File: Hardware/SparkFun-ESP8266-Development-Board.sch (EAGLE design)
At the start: 67 parts, among them J1 U.FL, Q1 2.5A/30V, Q2 MMBT2222A, U1 ESP8266, U2 MCP73831, U3 AT25SF041-SOIC8, U4 AP2112K-3.3V, U5 ATECC108-SSHDA, Y1 26MHz

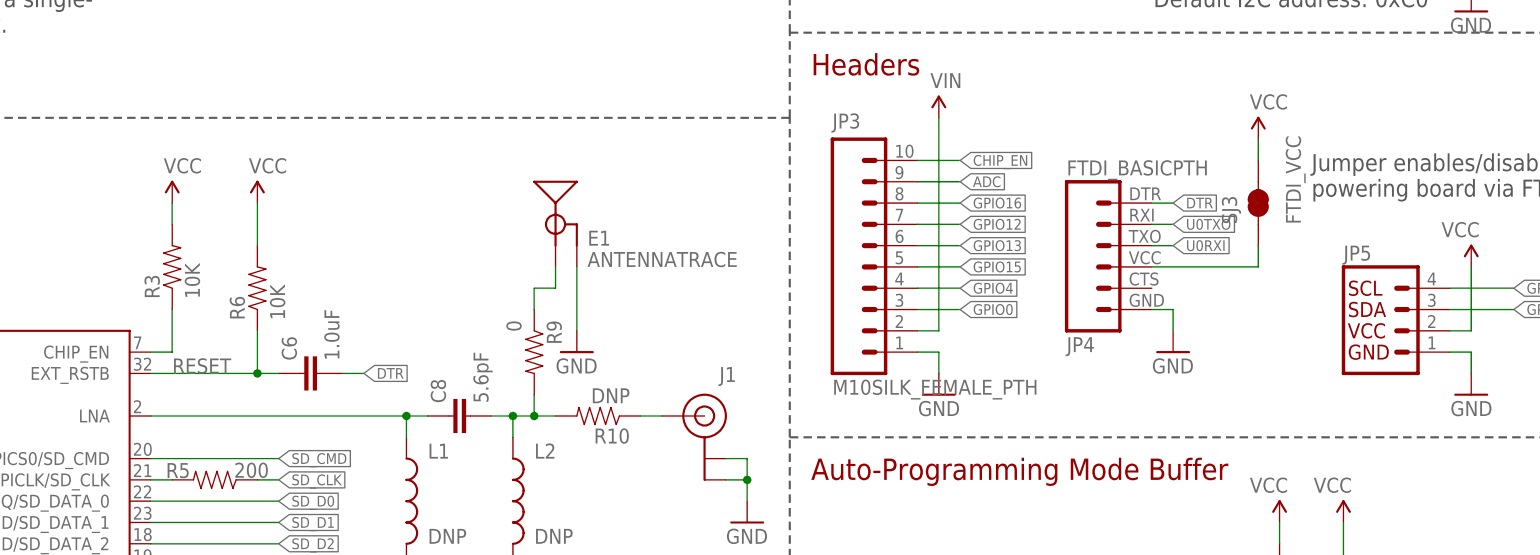
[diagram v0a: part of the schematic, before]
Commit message: Straightening out some nets coming out of ESP8266. Value JP5. Flag label on RESET.
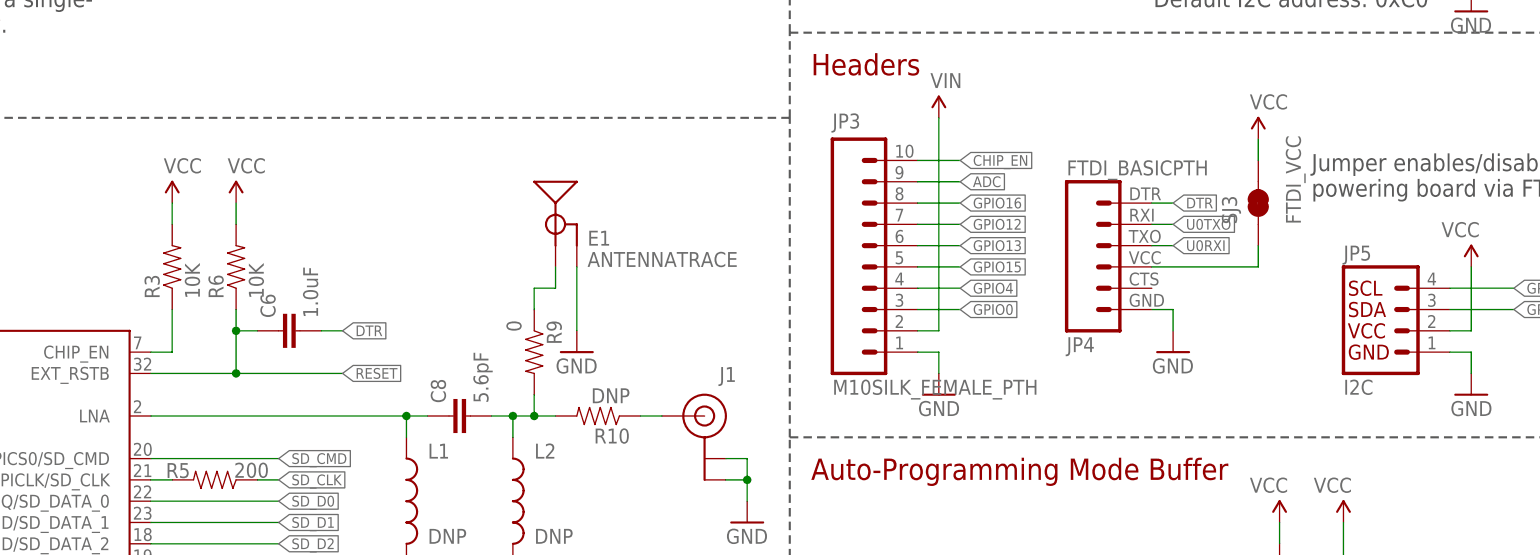
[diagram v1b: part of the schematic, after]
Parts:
- JP5: value (none) -> I2C
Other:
- moved on the sheet: C6, R6

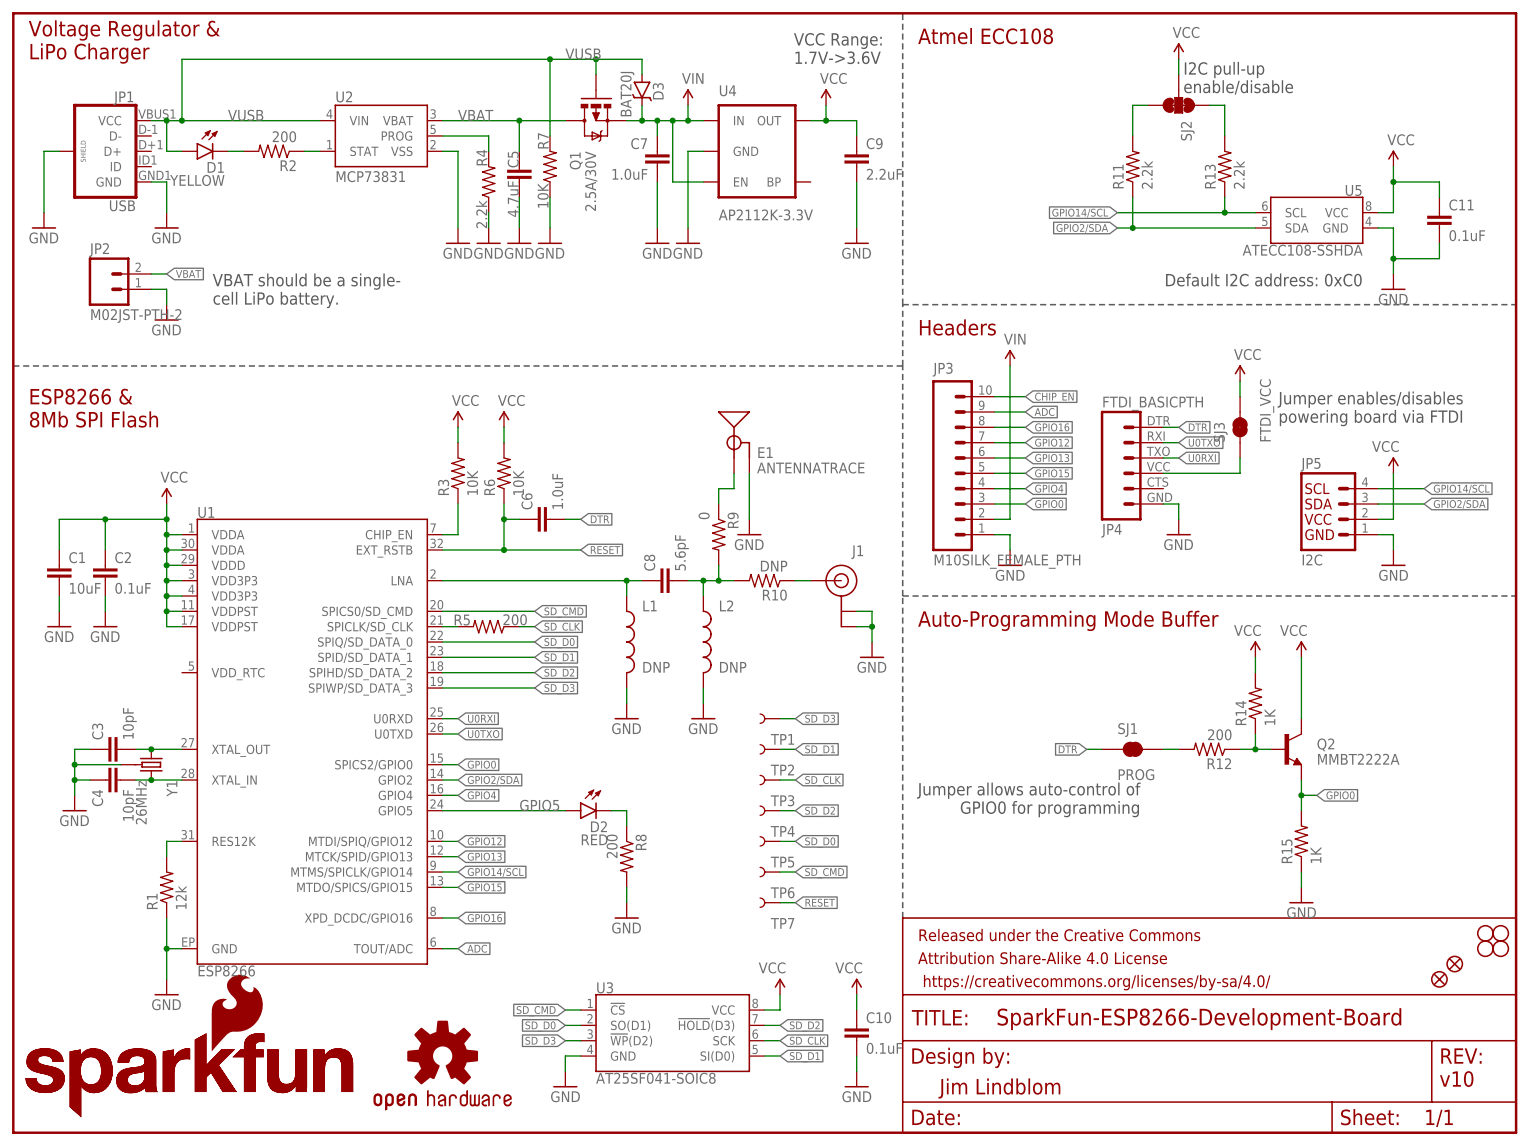
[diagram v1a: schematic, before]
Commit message: Adding power LED. Re-arranging power circuitry. Breaking out pin 5.
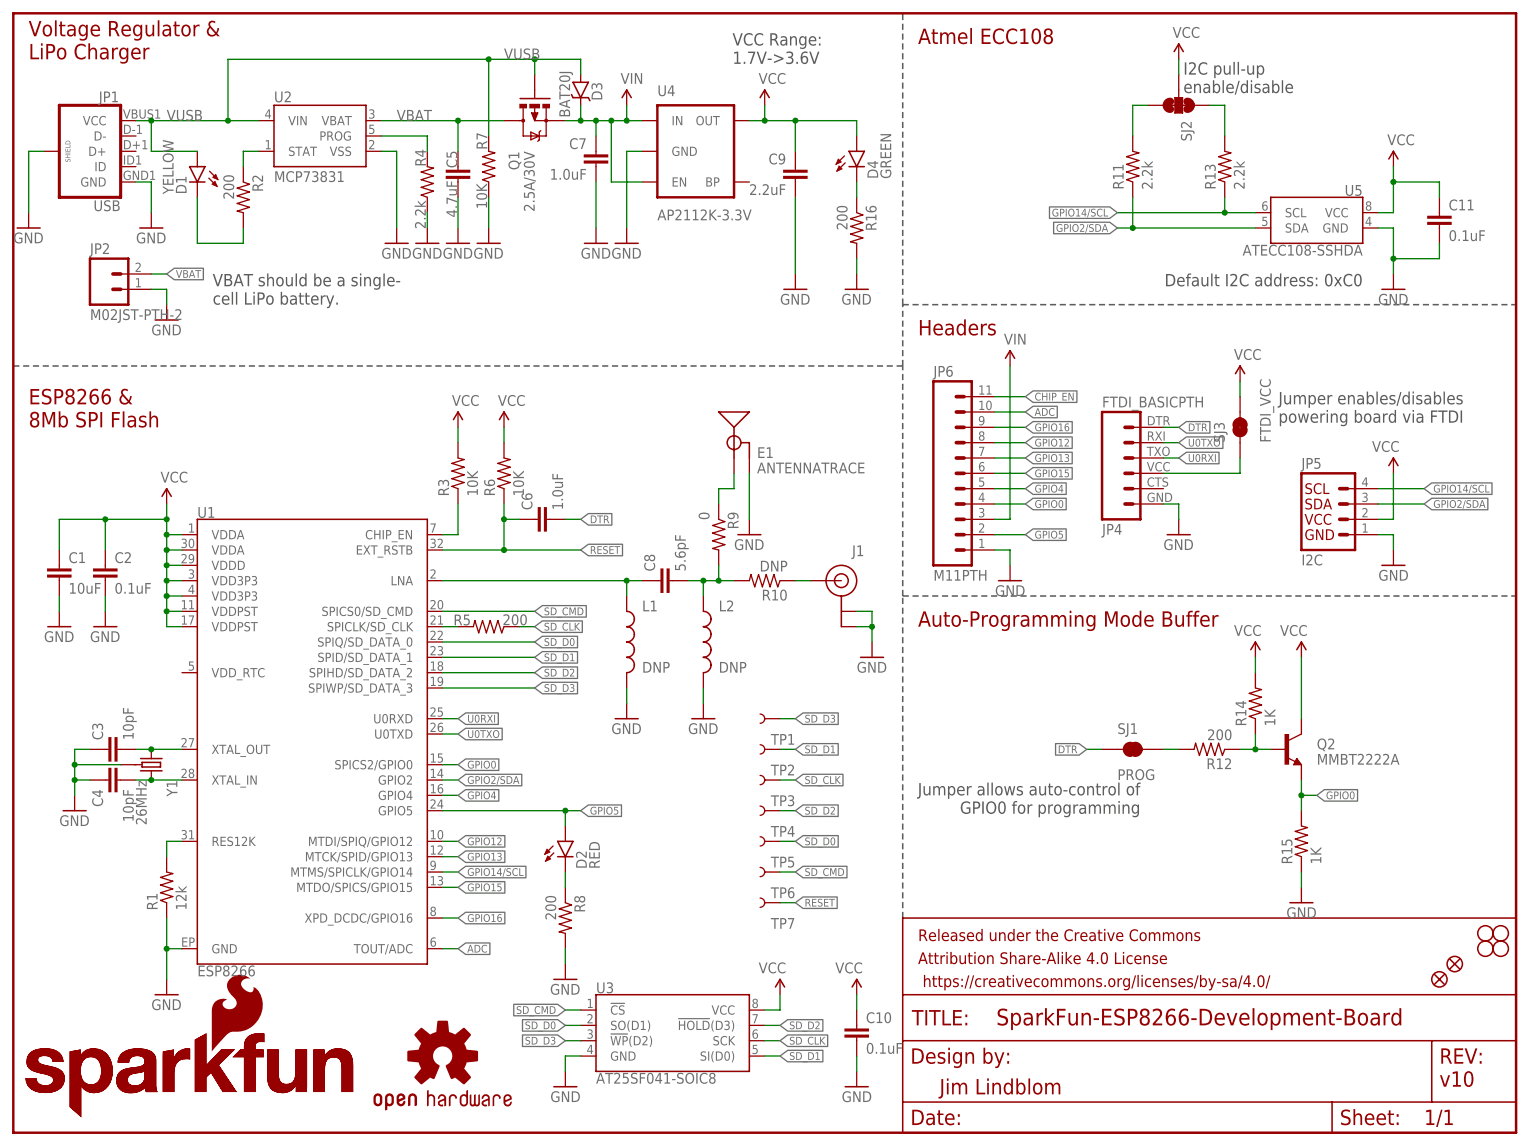
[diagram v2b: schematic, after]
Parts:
- removed JP3: M10SILK_FEMALE_PTH, SparkFun-Connectors:M10SILK_FEMALE_PTH
- added D4: GREEN, SparkFun-LED:LED-GREEN0603
- added JP6: M11PTH, SparkFun-Connectors:M11PTH
- added R16: 200, SparkFun-Resistors:200OHM1/10W1%(0603)
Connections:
- new net N$4: D4.C, R16.1
- net ADC: now also JP6.10; no longer JP3.9
- net CHIP_EN: now also JP6.11; no longer JP3.10
- net GND: now also JP6.1, R16.2; no longer JP3.1
- net GPIO0: now also JP6.4; no longer JP3.3
- net GPIO12: now also JP6.8; no longer JP3.7
- net GPIO13: now also JP6.7; no longer JP3.6
- net GPIO15: now also JP6.6; no longer JP3.5
- net GPIO16: now also JP6.9; no longer JP3.8
- net GPIO4: now also JP6.5; no longer JP3.4
- net GPIO5: now also JP6.2
- net VCC: now also D4.A
- net VIN: now also JP6.3; no longer JP3.2
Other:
- moved on the sheet: C5, C7, C9, D1, D2, D3, JP1, Q1, R2, R4, R7, R8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

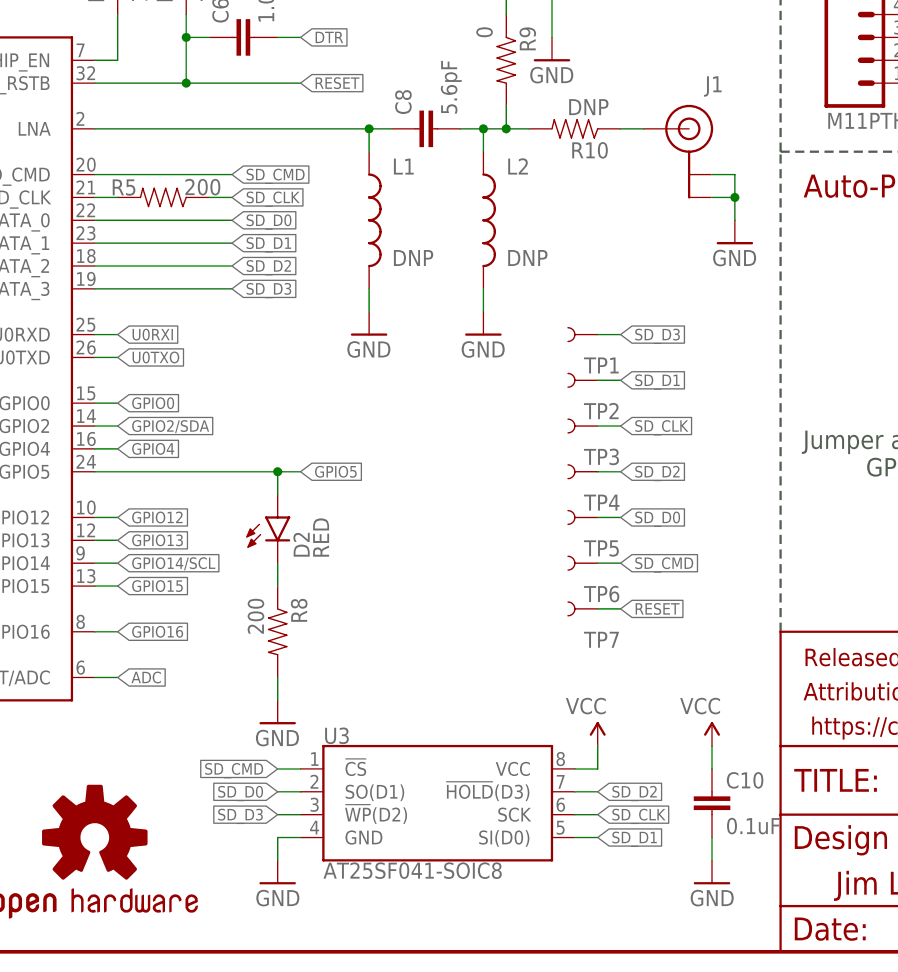
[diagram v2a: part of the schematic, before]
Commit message: Fixing net names for flash signals. Updating bottom silk labels
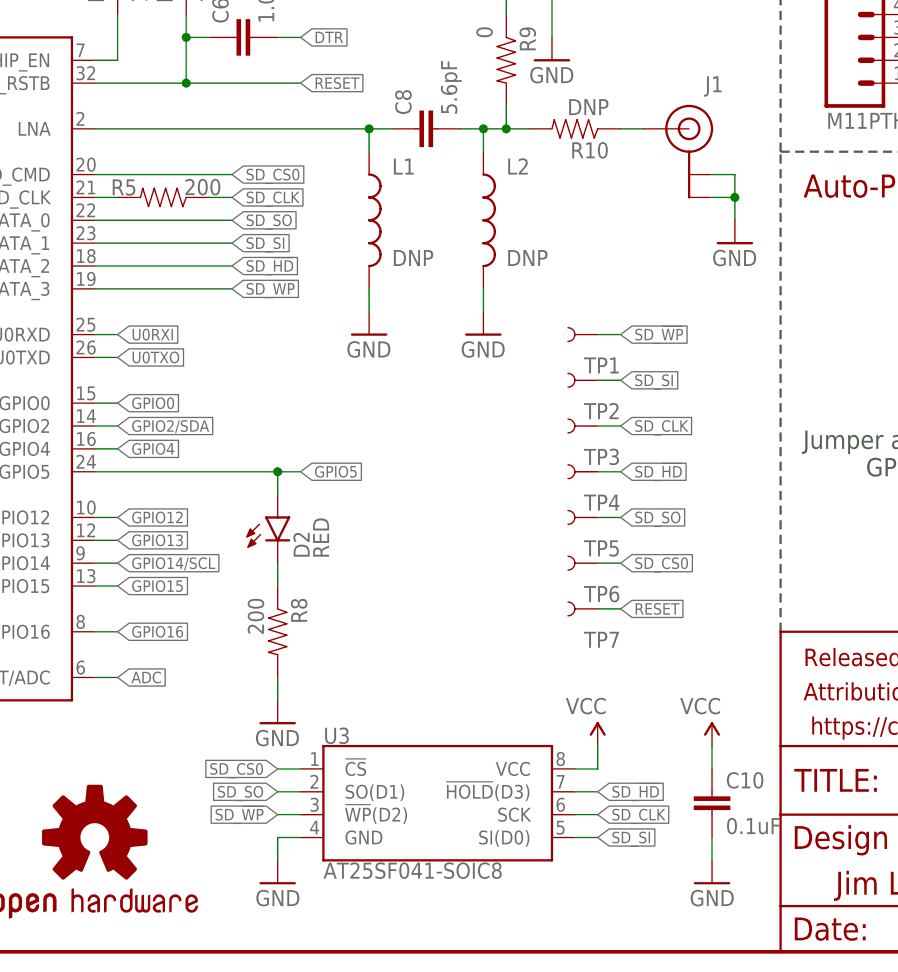
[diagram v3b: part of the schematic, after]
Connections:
- net SD_CMD renamed SD_CS0
- net SD_D0 renamed SD_SO
- net SD_D1 renamed SD_SI
- net SD_D2 renamed SD_!HD!
- net SD_D3 renamed SD_!WP!
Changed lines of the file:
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@@
 </segment>
 </net>
-<net name="SD_D3" class="0">
+<net name="SD_!WP!" class="0">
 <segment>
 <pinref part="U1" gate="G$1" pin="SPIWP/SD_DATA_3"/>
@@
 </segment>
 </net>
-<net name="SD_D2" class="0">
+<net name="SD_!HD!" class="0">
 <segment>
 <pinref part="U1" gate="G$1" pin="SPIHD/SD_DATA_2"/>
@@
 </segment>
 </net>
-<net name="SD_D1" class="0">
+<net name="SD_SI" class="0">
 <segment>
 <pinref part="U1" gate="G$1" pin="SPID/SD_DATA_1"/>
@@
 </segment>
 </net>
-<net name="SD_D0" class="0">
+<net name="SD_SO" class="0">
 <segment>
 <pinref part="U1" gate="G$1" pin="SPIQ/SD_DATA_0"/>
@@
 </segment>
 </net>
-<net name="SD_CMD" class="0">
+<net name="SD_CS0" class="0">
 <segment>
 <pinref part="U1" gate="G$1" pin="SPICS0/SD_CMD"/>
